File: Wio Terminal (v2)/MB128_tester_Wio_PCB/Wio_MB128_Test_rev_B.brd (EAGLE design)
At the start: 59.4 x 37.3 mm, 18 parts, among them IC1 SN74LVC2T45DCTR, IC2 SN74LVC2T45DCTR, IC3 SN74LVC2T45DCTR, J1 Joypad, J2 MD-80SGK, J3 CONN_20X2

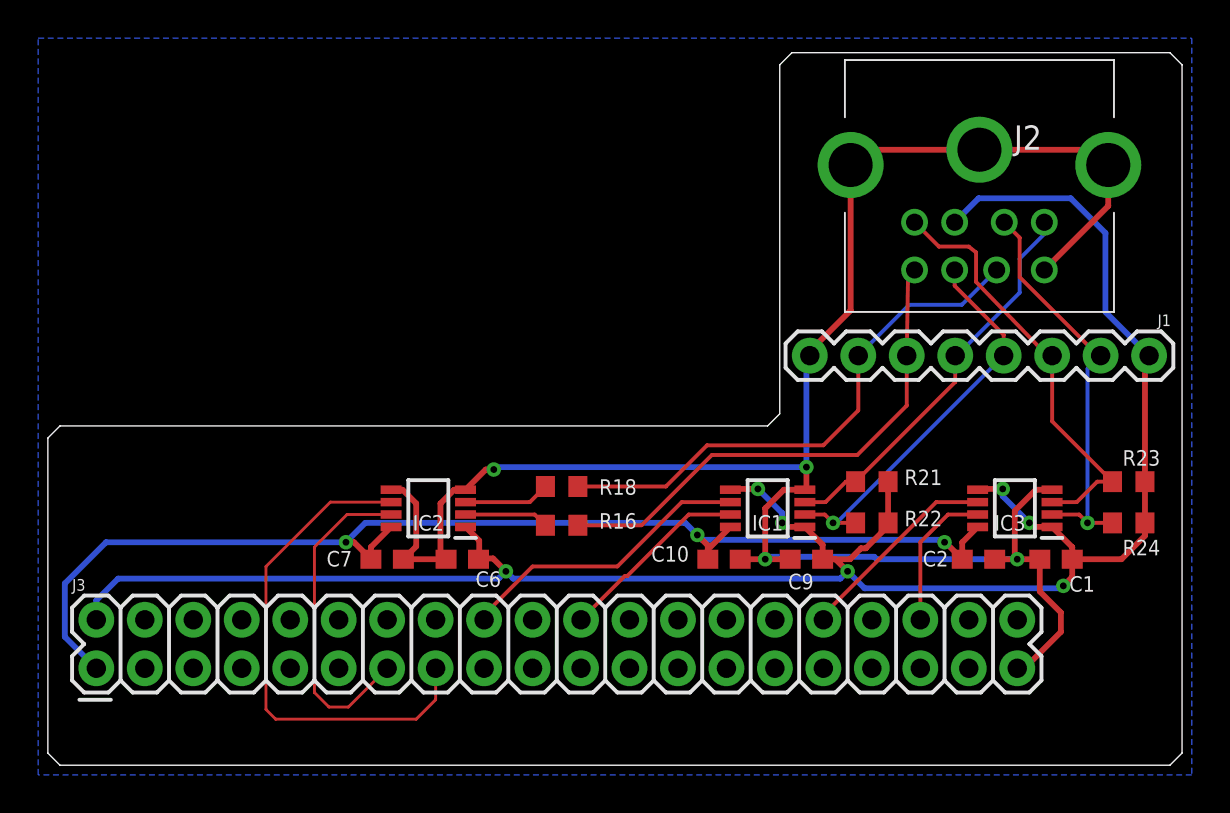
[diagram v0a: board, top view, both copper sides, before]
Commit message: Update board revision for Wio Terminal
- Update board revision for Wio Terminal, including the files required for JLCPCB to perform SMD assembly of the board.
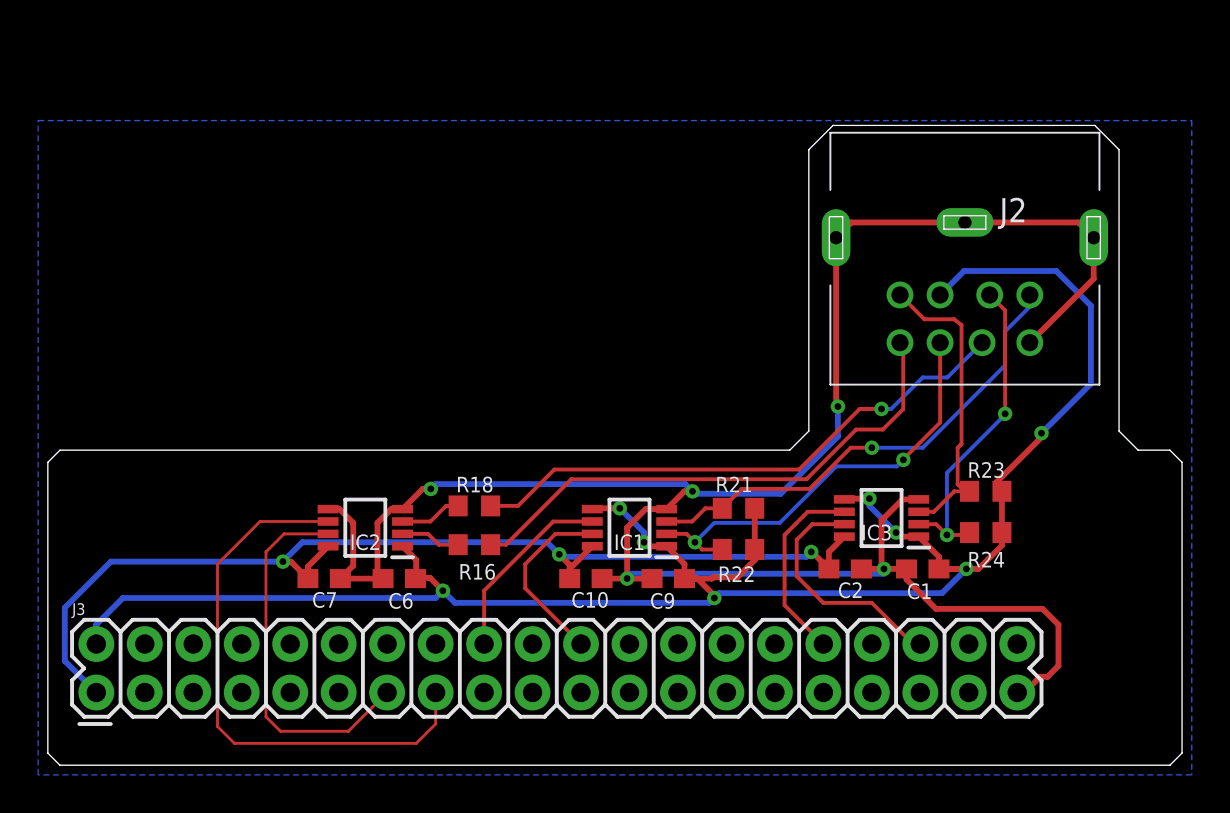
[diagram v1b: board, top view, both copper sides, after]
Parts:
- removed J1: Joypad, SparkFun-Connectors:1X08
- moved R23 7.51 mm to (49.1, 14.4)
- moved R24 7.51 mm to (49.1, 12.2)
- moved C10 7.31 mm to (28.2, 9.78)
- moved IC1 7.31 mm to (30.5, 12.4)
- moved C9 7.31 mm to (32.5, 9.78)
- moved R21 7.12 mm to (36.2, 13.5)
- moved R22 7.12 mm to (36.2, 11.3)
- moved C1 7.00 mm to (45.8, 10.3)
- moved C2 7.00 mm to (41.8, 10.3)
- moved IC3 7.00 mm to (43.7, 13.0)
- moved R16 4.68 mm to (22.4, 11.6)
- moved R18 4.68 mm to (22.4, 13.6)
- moved J2 3.89 mm to (48.1, 26.5)
- moved C7 3.45 mm to (14.5, 9.78)
- moved C6 3.45 mm to (18.4, 9.78)
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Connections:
- net +5V: no longer J1.1
- net CLR: no longer J1.7
- net GND: no longer J1.8
- net N$16: no longer J1.4
- net N$18: no longer J1.5
- net N$2: no longer J1.3
- net N$3: no longer J1.2
- net SEL: no longer J1.6
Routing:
- net GND: track 104.9 -> 113.1 mm, vias 4 -> 5
- net +3V3: track 63.8 -> 56.9 mm
- net +5V: track 111.0 -> 104.2 mm, vias 7 -> 8
- net N$2: track 22.6 -> 16.2 mm
- net N$8: track 15.6 -> 9.97 mm
- net N$33: track 7.67 -> 12.7 mm
- net N$18: track 20.8 -> 25.3 mm, vias 0 -> 1
- net N$3: track 21.6 -> 17.1 mm, vias 1 -> 2
- net N$1: track 17.3 -> 19.8 mm
- net N$4: track 26.6 -> 29.1 mm
- net N$16: track 21.0 -> 22.9 mm, vias 1 -> 2
- net N$21: track 4.52 -> 3.25 mm
- net N$13: track 4.42 -> 3.15 mm
- net SEL: track 27.1 -> 28.1 mm
- net CLR: track 28.3 -> 29.3 mm, vias 0 -> 1
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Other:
- board size 59.4 x 37.3 mm -> 59.4 x 33.5 mm
- board text added: "(C)2021 David Shadoff"
- board text removed: "(C)2020 David Shadoff"
- board text removed: "+5V"
- board text removed: "CLR"
- board text removed: "D0"
- board text removed: "D1"
- board text removed: "D2"
- board text removed: "D3"
- board text removed: "GND"
- board text removed: "SEL"
